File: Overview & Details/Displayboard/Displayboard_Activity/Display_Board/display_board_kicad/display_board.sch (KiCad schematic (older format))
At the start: 2 parts, among them J1 62684-502100ALF, U3 DISP_TFT_2.8IN_240x320_50PIN

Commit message: fixed symbol/footprint paths for displayboard
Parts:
- J1: symbol display_board:62684-502100ALF -> Display_Board:62684-502100ALF
- U3: symbol display_board:DISP_TFT_2.8IN_240x320_50PIN -> Display_Board:DISP_TFT_2.8IN_240x320_50PIN
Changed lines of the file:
@@
 $EndComp
 $Comp
-L display_board:62684-502100ALF J1
+L Display_Board:62684-502100ALF J1
 U 1 1 5F061D23
 P 6000 1420
@@
 $EndComp
 $Comp
-L display_board:DISP_TFT_2.8IN_240x320_50PIN U3
+L Display_Board:DISP_TFT_2.8IN_240x320_50PIN U3
 U 1 1 5F053F83
 P 3190 2900

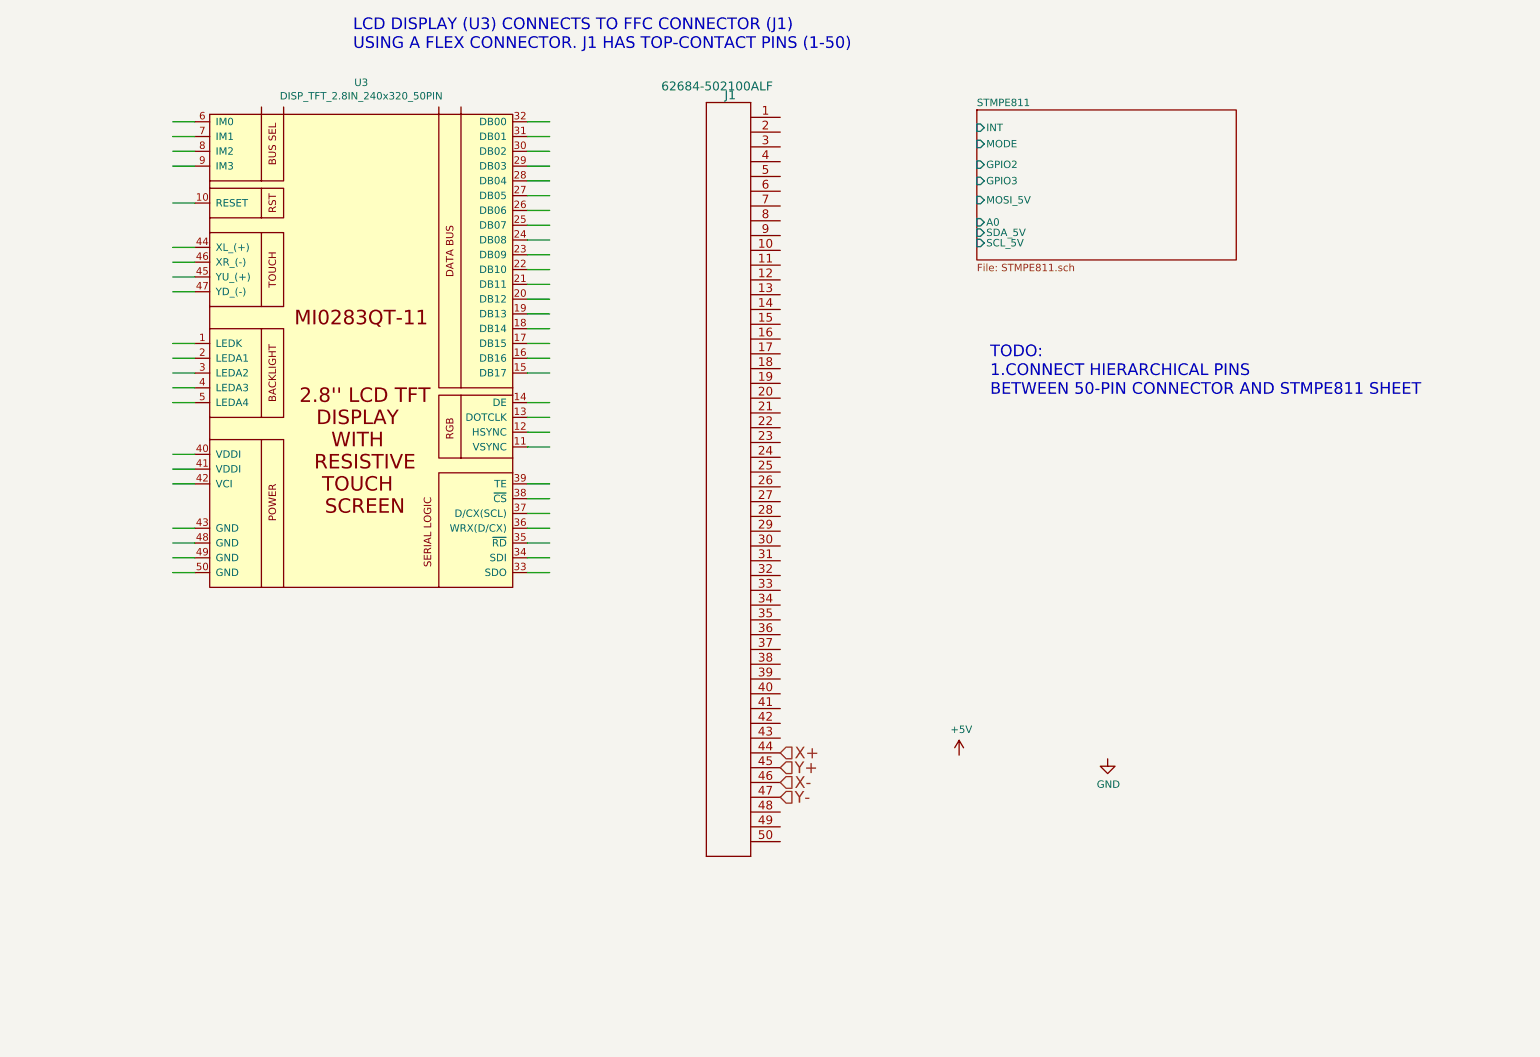
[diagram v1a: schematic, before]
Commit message: created footprint for circular pins for sam32 and linked to symbols. linked displayboard's lcd screen to the 50pin connector footprint
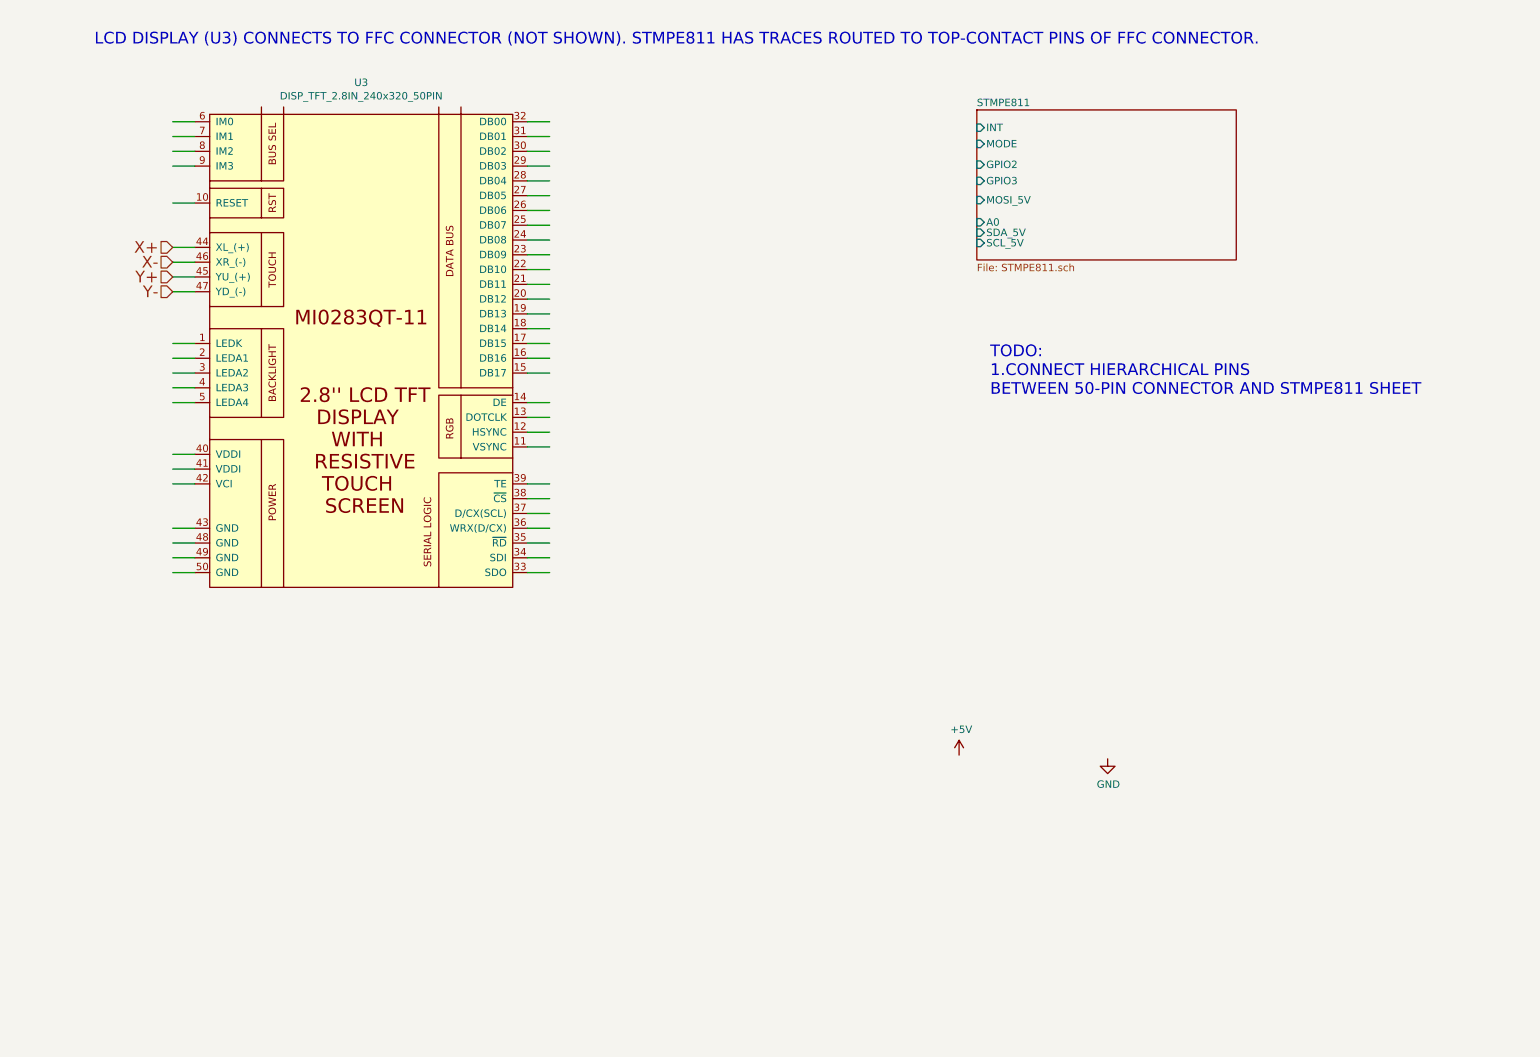
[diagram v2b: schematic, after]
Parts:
- removed J1: 62684-502100ALF, Display_Board:62684-502100ALF, symbol Display_Board:62684-502100ALF
- U3: footprint (none) -> Display_Board:62684-502100ALF
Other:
- note added: "LCD DISPLAY (U3) CONNECTS TO FFC CONNECTOR (NOT SHOWN). STMPE811 HAS TRACES ROUTED TO TOP-CONTACT PINS OF FFC CONNECTOR.\n"
- note removed: "LCD DISPLAY (U3) CONNECTS TO FFC CONNECTOR (J1) \nUSING A FLEX CONNECTOR. J1 HAS TOP-CONTACT PINS (1-50)"
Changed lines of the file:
@@
-$EndComp
-$Comp
-L Display_Board:62684-502100ALF J1
-U 1 1 5F061D23
-P 6000 1420
-F 0 "J1" H 6300 1570 60  0000 L CNN
-F 1 "62684-502100ALF" H 6050 1630 60  0000 L CNN
-F 2 "Display_Board:62684-502100ALF" H 6400 -1040 60  0001 C CNN
-F 3 "" H 6000 1420 60  0000 C CNN
-	1    6000 1420
-	-1   0    0    -1
 $EndComp
 $Comp
@@
 F 0 "U3" H 3165 4615 50  0000 C CNN
 F 1 "DISP_TFT_2.8IN_240x320_50PIN" H 3165 4524 50  0000 C CNN
-F 2 "" H 3340 2900 50  0001 C CNN
+F 2 "Display_Board:62684-502100ALF" H 3340 2900 50  0001 C CNN
 F 3 "" H 3340 2900 50  0001 C CNN
 	1    3190 2900
@@
 Wire Wire Line
 	1890 4200 2040 4200
-Text Notes 3110 970  0    79   ~ 0
-LCD DISPLAY (U3) CONNECTS TO FFC CONNECTOR (J1) \nUSING A FLEX CONNECTOR. J1 HAS TOP-CONTACT PINS (1-50)
-Text HLabel 6000 5720 2    79   Input ~ 0
-X+
-Text HLabel 6000 5820 2    79   Input ~ 0
-Y+
-Text HLabel 6000 5920 2    79   Input ~ 0
-X-
-Text HLabel 6000 6020 2    79   Input ~ 0
-Y-
+Text Notes 1360 940  0    79   ~ 0
+LCD DISPLAY (U3) CONNECTS TO FFC CONNECTOR (NOT SHOWN). STMPE811 HAS TRACES ROUTED TO TOP-CONTACT PINS OF FFC CONNECTOR.\n
 Text Notes 7420 3310 0    79   ~ 0
 TODO:\n1.CONNECT HIERARCHICAL PINS\nBETWEEN 50-PIN CONNECTOR AND STMPE811 SHEET
+Text HLabel 1890 2300 0    79   Input ~ 0
+X+
+Text HLabel 1890 2500 0    79   Input ~ 0
+Y+
+Text HLabel 1890 2400 0    79   Input ~ 0
+X-
+Text HLabel 1890 2600 0    79   Input ~ 0
+Y-
 $EndSCHEMATC

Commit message: displayboard WIP
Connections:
- net labels removed: X+, X-, Y+, Y-
- wire segments 50 -> 64
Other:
- note added: "TODO:\n1.CONNECT HIERARCHICAL PINS\nBETWEEN 50-PIN CONNECTOR (THE SYMBOL ON THE RIGHT)\nAND STMPE811 SHEET"
- note removed: "TODO:\n1.CONNECT HIERARCHICAL PINS\nBETWEEN 50-PIN CONNECTOR AND STMPE811 SHEET"
- moved on the sheet: U3
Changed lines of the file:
@@
 Comment4 ""
 $EndDescr
+$Comp
+L power:GND #PWR03
+U 1 1 5EE95F40
+P 6485 7470
+F 0 "#PWR03" H 6485 7220 50  0001 C CNN
+F 1 "GND" H 6490 7297 50  0000 C CNN
+F 2 "" H 6485 7470 50  0001 C CNN
+F 3 "" H 6485 7470 50  0001 C CNN
+	1    6485 7470
+	1    0    0    -1
+$EndComp
+$Comp
+L power:+5V #PWR02
+U 1 1 5EEF5BFF
+P 6250 7585
+F 0 "#PWR02" H 6250 7435 50  0001 C CNN
+F 1 "+5V" H 6265 7758 50  0000 C CNN
+F 2 "" H 6250 7585 50  0001 C CNN
+F 3 "" H 6250 7585 50  0001 C CNN
+	1    6250 7585
+	1    0    0    -1
+$EndComp
+$Comp
+L Display_Board:DISP_TFT_2.8IN_240x320_50PIN U3
+U 1 1 5F053F83
+P 6360 4470
+F 0 "U3" H 6335 6185 50  0000 C CNN
+F 1 "DISP_TFT_2.8IN_240x320_50PIN" H 6335 6094 50  0000 C CNN
+F 2 "Display_Board:62684-502100ALF" H 6510 4470 50  0001 C CNN
+F 3 "" H 6510 4470 50  0001 C CNN
+	1    6360 4470
+	1    0    0    -1
+$EndComp
+Wire Wire Line
+	7460 6070 7610 6070
+Wire Wire Line
+	7460 5970 7610 5970
+Wire Wire Line
+	7460 5870 7610 5870
+Wire Wire Line
+	7460 5770 7610 5770
+Wire Wire Line
+	7460 5570 7610 5570
+Wire Wire Line
+	7460 5470 7610 5470
+Wire Wire Line
+	7460 5220 7610 5220
+Wire Wire Line
+	7460 5120 7610 5120
+Wire Wire Line
+	7460 5020 7610 5020
+Wire Wire Line
+	7460 4920 7610 4920
+Wire Wire Line
+	7460 4720 7610 4720
+Wire Wire Line
+	7460 4620 7610 4620
+Wire Wire Line
+	7460 4520 7610 4520
+Wire Wire Line
+	7460 4420 7610 4420
+Wire Wire Line
+	7460 4320 7610 4320
+Wire Wire Line
+	7460 4220 7610 4220
+Wire Wire Line
+	7460 4120 7610 4120
+Wire Wire Line
+	7460 4020 7610 4020
+Wire Wire Line
+	7460 3920 7610 3920
+Wire Wire Line
+	7460 3820 7610 3820
+Wire Wire Line
+	7460 3720 7610 3720
+Wire Wire Line
+	7460 3620 7610 3620
+Wire Wire Line
+	7460 3520 7610 3520
+Wire Wire Line
+	7460 3420 7610 3420
+Wire Wire Line
+	7460 3320 7610 3320
+Wire Wire Line
+	7460 3220 7610 3220
+Wire Wire Line
+	7460 3120 7610 3120
+Wire Wire Line
+	7460 3020 7610 3020
+Wire Wire Line
+	5060 3220 5210 3220
+Wire Wire Line
+	5060 3120 5210 3120
+Wire Wire Line
+	5060 3020 5210 3020
+Wire Wire Line
+	5060 4520 5210 4520
+Wire Wire Line
+	5060 3570 5210 3570
+Wire Wire Line
+	5060 3320 5210 3320
+Wire Wire Line
+	5060 5470 5210 5470
+Wire Wire Line
+	5060 5370 5210 5370
+Wire Wire Line
+	5060 5270 5210 5270
+Wire Wire Line
+	5060 4920 5210 4920
+Wire Wire Line
+	5060 4820 5210 4820
+Wire Wire Line
+	5060 4720 5210 4720
+Wire Wire Line
+	5060 4620 5210 4620
+Wire Wire Line
+	5060 6070 5210 6070
+Wire Wire Line
+	5060 5970 5210 5970
+Wire Wire Line
+	5060 5870 5210 5870
+Wire Wire Line
+	5060 5770 5210 5770
+Text Notes 1360 940  0    79   ~ 0
+LCD DISPLAY (U3) CONNECTS TO FFC CONNECTOR (NOT SHOWN). STMPE811 HAS TRACES ROUTED TO TOP-CONTACT PINS OF FFC CONNECTOR.\n
+Text Notes 800  3390 0    79   ~ 0
+TODO:\n1.CONNECT HIERARCHICAL PINS\nBETWEEN 50-PIN CONNECTOR (THE SYMBOL ON THE RIGHT)\nAND STMPE811 SHEET
+Wire Wire Line
+	5060 5770 5060 5870
+Wire Wire Line
+	5060 5970 5060 5870
+Connection ~ 5060 5870
+Wire Wire Line
+	5060 5970 5060 6070
+Connection ~ 5060 5970
+Wire Wire Line
+	5060 6070 5060 6310
+Connection ~ 5060 6070
+$Comp
+L power:GND #PWR?
+U 1 1 5EBC77CE
+P 5060 6310
+F 0 "#PWR?" H 5060 6060 50  0001 C CNN
+F 1 "GND" H 5065 6137 50  0000 C CNN
+F 2 "" H 5060 6310 50  0001 C CNN
+F 3 "" H 5060 6310 50  0001 C CNN
+	1    5060 6310
+	1    0    0    -1
+$EndComp
+Wire Wire Line
+	4960 3870 5210 3870
+Wire Wire Line
+	4960 2170 4960 3870
+Wire Wire Line
+	4620 3970 4620 2090
+Wire Wire Line
+	4620 3970 5210 3970
+Wire Wire Line
+	4900 4070 4900 2330
+Wire Wire Line
+	4900 4070 5210 4070
+Wire Wire Line
+	4760 2250 4760 4170
+Wire Wire Line
+	4760 4170 5210 4170
+Wire Wire Line
+	5060 2250 4760 2250
+Wire Wire Line
+	4900 2330 5060 2330
+Wire Wire Line
+	4620 2090 5060 2090
+Wire Wire Line
+	4960 2170 5060 2170
 $Sheet
-S 7330 1370 1755 1015
+S 5060 1370 1755 1015
 U 5E88FA4B
 F0 "STMPE811" 50
 F1 "STMPE811.sch" 50
-F2 "INT" I L 7330 1490 50
-F3 "MODE" I L 7330 1600 50
-F4 "GPIO2" I L 7330 1740 50
-F5 "GPIO3" I L 7330 1850 50
-F6 "MOSI_5V" I L 7330 1980 50
-F7 "A0" I L 7330 2130 50
-F8 "SCL_5V" I L 7330 2270 50
-F9 "SDA_5V" I L 7330 2200 50
+F2 "GPIO2" I L 5060 1420 50
+F3 "GPIO3" I L 5060 1520 50
+F4 "MODE" I R 6815 1420 50
+F5 "MOSI_5V" I R 6815 1500 50
+F6 "A0" I R 6815 1580 50
+F7 "INT" I R 6815 1670 50
+F8 "SCL_5V" I R 6815 1760 50
+F9 "SDA_5V" I R 6815 1850 50
+F10 "Y+" B L 5060 2330 50
+F11 "Y-" B L 5060 2250 50
+F12 "X+" B L 5060 2170 50
+F13 "X-" B L 5060 2090 50
 $EndSheet
-$Comp
-L power:GND #PWR03
-U 1 1 5EE95F40
-P 8215 5760
-F 0 "#PWR03" H 8215 5510 50  0001 C CNN
-F 1 "GND" H 8220 5587 50  0000 C CNN
-F 2 "" H 8215 5760 50  0001 C CNN
-F 3 "" H 8215 5760 50  0001 C CNN
-	1    8215 5760
-	1    0    0    -1
-$EndComp
-$Comp
-L power:+5V #PWR02
-U 1 1 5EEF5BFF
-P 7210 5735
-F 0 "#PWR02" H 7210 5585 50  0001 C CNN
-F 1 "+5V" H 7225 5908 50  0000 C CNN
-F 2 "" H 7210 5735 50  0001 C CNN
-F 3 "" H 7210 5735 50  0001 C CNN
-	1    7210 5735
-	1    0    0    -1
-$EndComp
-$Comp
-L Display_Board:DISP_TFT_2.8IN_240x320_50PIN U3
-U 1 1 5F053F83
-P 3190 2900
-F 0 "U3" H 3165 4615 50  0000 C CNN
-F 1 "DISP_TFT_2.8IN_240x320_50PIN" H 3165 4524 50  0000 C CNN
-F 2 "Display_Board:62684-502100ALF" H 3340 2900 50  0001 C CNN
-F 3 "" H 3340 2900 50  0001 C CNN
-	1    3190 2900
-	1    0    0    -1
-$EndComp
-Wire Wire Line
-	4290 4500 4440 4500
-Wire Wire Line
-	4290 4400 4440 4400
-Wire Wire Line
-	4290 4300 4440 4300
-Wire Wire Line
-	4290 4200 4440 4200
-Wire Wire Line
-	4290 4100 4440 4100
-Wire Wire Line
-	4290 4000 4440 4000
-Wire Wire Line
-	4290 3900 4440 3900
-Wire Wire Line
-	4290 3650 4440 3650
-Wire Wire Line
-	4290 3550 4440 3550
-Wire Wire Line
-	4290 3450 4440 3450
-Wire Wire Line
-	4290 3350 4440 3350
-Wire Wire Line
-	4290 3150 4440 3150
-Wire Wire Line
-	4290 3050 4440 3050
-Wire Wire Line
-	4290 2950 4440 2950
-Wire Wire Line
-	4290 2850 4440 2850
-Wire Wire Line
-	4290 2750 4440 2750
-Wire Wire Line
-	4290 2650 4440 2650
-Wire Wire Line
-	4290 2550 4440 2550
-Wire Wire Line
-	4290 2450 4440 2450
-Wire Wire Line
-	4290 2350 4440 2350
-Wire Wire Line
-	4290 2250 4440 2250
-Wire Wire Line
-	4290 2150 4440 2150
-Wire Wire Line
-	4290 2050 4440 2050
-Wire Wire Line
-	4290 1950 4440 1950
-Wire Wire Line
-	4290 1850 4440 1850
-Wire Wire Line
-	4290 1750 4440 1750
-Wire Wire Line
-	4290 1650 4440 1650
-Wire Wire Line
-	4290 1550 4440 1550
-Wire Wire Line
-	4290 1450 4440 1450
-Wire Wire Line
-	1890 1650 2040 1650
-Wire Wire Line
-	1890 1550 2040 1550
-Wire Wire Line
-	1890 1450 2040 1450
-Wire Wire Line
-	1890 2950 2040 2950
-Wire Wire Line
-	1890 2600 2040 2600
-Wire Wire Line
-	1890 2500 2040 2500
-Wire Wire Line
-	1890 2400 2040 2400
-Wire Wire Line
-	1890 2300 2040 2300
-Wire Wire Line
-	1890 2000 2040 2000
-Wire Wire Line
-	1890 1750 2040 1750
-Wire Wire Line
-	1890 3900 2040 3900
-Wire Wire Line
-	1890 3800 2040 3800
-Wire Wire Line
-	1890 3700 2040 3700
-Wire Wire Line
-	1890 3350 2040 3350
-Wire Wire Line
-	1890 3250 2040 3250
-Wire Wire Line
-	1890 3150 2040 3150
-Wire Wire Line
-	1890 3050 2040 3050
-Wire Wire Line
-	1890 4500 2040 4500
-Wire Wire Line
-	1890 4400 2040 4400
-Wire Wire Line
-	1890 4300 2040 4300
-Wire Wire Line
-	1890 4200 2040 4200
-Text Notes 1360 940  0    79   ~ 0
-LCD DISPLAY (U3) CONNECTS TO FFC CONNECTOR (NOT SHOWN). STMPE811 HAS TRACES ROUTED TO TOP-CONTACT PINS OF FFC CONNECTOR.\n
-Text Notes 7420 3310 0    79   ~ 0
-TODO:\n1.CONNECT HIERARCHICAL PINS\nBETWEEN 50-PIN CONNECTOR AND STMPE811 SHEET
-Text HLabel 1890 2300 0    79   Input ~ 0
-X+
-Text HLabel 1890 2500 0    79   Input ~ 0
-Y+
-Text HLabel 1890 2400 0    79   Input ~ 0
-X-
-Text HLabel 1890 2600 0    79   Input ~ 0
-Y-
+Wire Wire Line
+	6815 1760 8400 1760
+Wire Wire Line
+	8400 1760 8400 5670
+Wire Wire Line
+	7460 5670 8400 5670
 $EndSCHEMATC
